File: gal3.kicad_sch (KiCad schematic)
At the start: 4 parts, among them IC13 SN74ALS374N, IC9 D65200GD076

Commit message: wire IC13
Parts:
- added C60: C_Small, Capacitor_SMD:C_1206_3216Metric, symbol Device:C_Small
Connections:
- net +5V: now also C60.1
- net GND: now also C60.2
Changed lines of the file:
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@@
   (junction (at 144.78 166.37) (diameter 0) (color 0 0 0 0)
+  )
+  (junction (at 95.25 137.16) (diameter 0) (color 0 0 0 0)
   )
   (junction (at 149.86 156.21) (diameter 0) (color 0 0 0 0)
@@
     (stroke (width 0) (type default))
   )
+  (wire (pts (xy 86.36 137.16) (xy 95.25 137.16))
+    (stroke (width 0) (type default))
+  )
   (wire (pts (xy 107.95 171.45) (xy 118.11 171.45))
     (stroke (width 0) (type default))
@@
     (stroke (width 0) (type default))
   )
+  (wire (pts (xy 86.36 140.97) (xy 86.36 142.24))
+    (stroke (width 0) (type default))
+  )
   (wire (pts (xy 139.7 151.13) (xy 167.64 151.13))
     (stroke (width 0) (type default))
@@
     (stroke (width 0) (type default))
   )
+  (wire (pts (xy 95.25 137.16) (xy 95.25 143.51))
+    (stroke (width 0) (type default))
+  )
   (wire (pts (xy 144.78 166.37) (xy 167.64 166.37))
     (stroke (width 0) (type default))
@@
   )
   (wire (pts (xy 152.4 142.24) (xy 152.4 158.75))
+    (stroke (width 0) (type default))
+  )
+  (wire (pts (xy 95.25 135.89) (xy 95.25 137.16))
     (stroke (width 0) (type default))
   )
@@
     )
   )
+  (symbol (lib_id "power:GND") (at 86.36 140.97 0) (unit 1)
+    (in_bom yes) (on_board yes) (dnp no) (fields_autoplaced)
+    (property "Reference" "#PWR034" (at 86.36 147.32 0)
+      (effects (font (size 1.27 1.27)) hide)
+    )
+    (property "Value" "GND" (at 86.36 146.05 0)
+      (effects (font (size 1.27 1.27)))
+    )
+    (property "Footprint" "" (at 86.36 140.97 0)
+      (effects (font (size 1.27 1.27)) hide)
+    )
+    (property "Datasheet" "" (at 86.36 140.97 0)
+      (effects (font (size 1.27 1.27)) hide)
+    )
+    (pin "1")
+    (instances
+      (project "88va2-circuit"
+        (path "/8cd193ae-a369-4130-9ba4-f2075fa60e2b/69b5e096-b79d-4084-a9d7-aa17e9aa2515"
+          (reference "#PWR034") (unit 1)
+        )
+      )
+    )
+  )
   (symbol (lib_id "power:+5V") (at 52.07 72.39 0) (unit 1)
     (in_bom yes) (on_board yes) (dnp no) (fields_autoplaced)
@@
     )
   )
+  (symbol (lib_id "Device:C_Small") (at 86.36 139.7 0) (unit 1)
+    (in_bom yes) (on_board yes) (dnp no) (fields_autoplaced)
+    (property "Reference" "C60" (at 88.9 139.7063 0)
+      (effects (font (size 1.27 1.27)) (justify left))
+    )
+    (property "Value" "C_Small" (at 88.9 140.9763 0)
+      (effects (font (size 1.27 1.27)) (justify left) hide)
+    )
+    (property "Footprint" "Capacitor_SMD:C_1206_3216Metric" (at 86.36 139.7 0)
+      (effects (font (size 1.27 1.27)) hide)
+    )
+    (property "Datasheet" "~" (at 86.36 139.7 0)
+      (effects (font (size 1.27 1.27)) hide)
+    )
+    (pin "2")
+    (pin "1")
+    (instances
+      (project "88va2-circuit"
+        (path "/8cd193ae-a369-4130-9ba4-f2075fa60e2b/69b5e096-b79d-4084-a9d7-aa17e9aa2515"
+          (reference "C60") (unit 1)
+        )
+      )
+    )
+  )
   (symbol (lib_id "power:+5V") (at 137.16 132.08 0) (unit 1)
     (in_bom yes) (on_board yes) (dnp no) (fields_autoplaced)
@@
     )
   )
-  (symbol (lib_id "power:+5V") (at 95.25 143.51 0) (unit 1)
-    (in_bom yes) (on_board yes) (dnp no) (fields_autoplaced)
-    (property "Reference" "#PWR032" (at 95.25 147.32 0)
-      (effects (font (size 1.27 1.27)) hide)
-    )
-    (property "Value" "+5V" (at 95.25 138.43 0)
+  (symbol (lib_id "power:+5V") (at 95.25 135.89 0) (unit 1)
+    (in_bom yes) (on_board yes) (dnp no) (fields_autoplaced)
+    (property "Reference" "#PWR032" (at 95.25 139.7 0)
+      (effects (font (size 1.27 1.27)) hide)
+    )
+    (property "Value" "+5V" (at 95.25 130.81 0)
       (effects (font (size 1.27 1.27)))
     )
-    (property "Footprint" "" (at 95.25 143.51 0)
-      (effects (font (size 1.27 1.27)) hide)
-    )
-    (property "Datasheet" "" (at 95.25 143.51 0)
-      (effects (font (size 1.27 1.27)) hide)
-    )
+    (property "Footprint" "" (at 95.25 135.89 0)
+      (effects (font (size 1.27 1.27)) hide)
+    )
+    (property "Datasheet" "" (at 95.25 135.89 0)
+      (effects (font (size 1.27 1.27)) hide)
+    )

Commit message: wire IC13
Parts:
- R18: footprint (none) -> Resistor_SMD:R_1206_3216Metric
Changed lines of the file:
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@@
       (effects (font (size 1.27 1.27)) (justify left) hide)
     )
-    (property "Footprint" "" (at 72.39 143.51 0)
+    (property "Footprint" "Resistor_SMD:R_1206_3216Metric" (at 72.39 143.51 0)
       (effects (font (size 1.27 1.27)) hide)
     )

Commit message: fix pitch of IC9 pads
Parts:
- IC9: footprint 88va_Library:QFP-160_28x28_Pitch0.635mm -> 88va_Library:QFP-160_27.8x27.8_Pitch0.65mm
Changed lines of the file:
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@@
       (effects (font (size 1.27 1.27)) (justify left))
     )
-    (property "Footprint" "88va_Library:QFP-160_28x28_Pitch0.635mm" (at 52.07 78.74 0)
+    (property "Footprint" "88va_Library:QFP-160_27.8x27.8_Pitch0.65mm" (at 52.07 78.74 0)
       (effects (font (size 1.27 1.27)) hide)
     )

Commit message: wire power lines
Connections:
- net +5V: now also IC9.1 (VDD); no longer IC9.81 (VDD)
- net GND: now also IC9.41 (GND), IC9.42 (GND); no longer IC9.79 (GND), IC9.80 (GND)
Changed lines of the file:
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@@
     (pin "44")
     (pin "50")
-    (pin "80")
+    (pin "1")
     (pin "48")
     (pin "51")
-    (pin "79")
-    (pin "81")
+    (pin "41")
+    (pin "42")
     (pin "69")
     (pin "140")

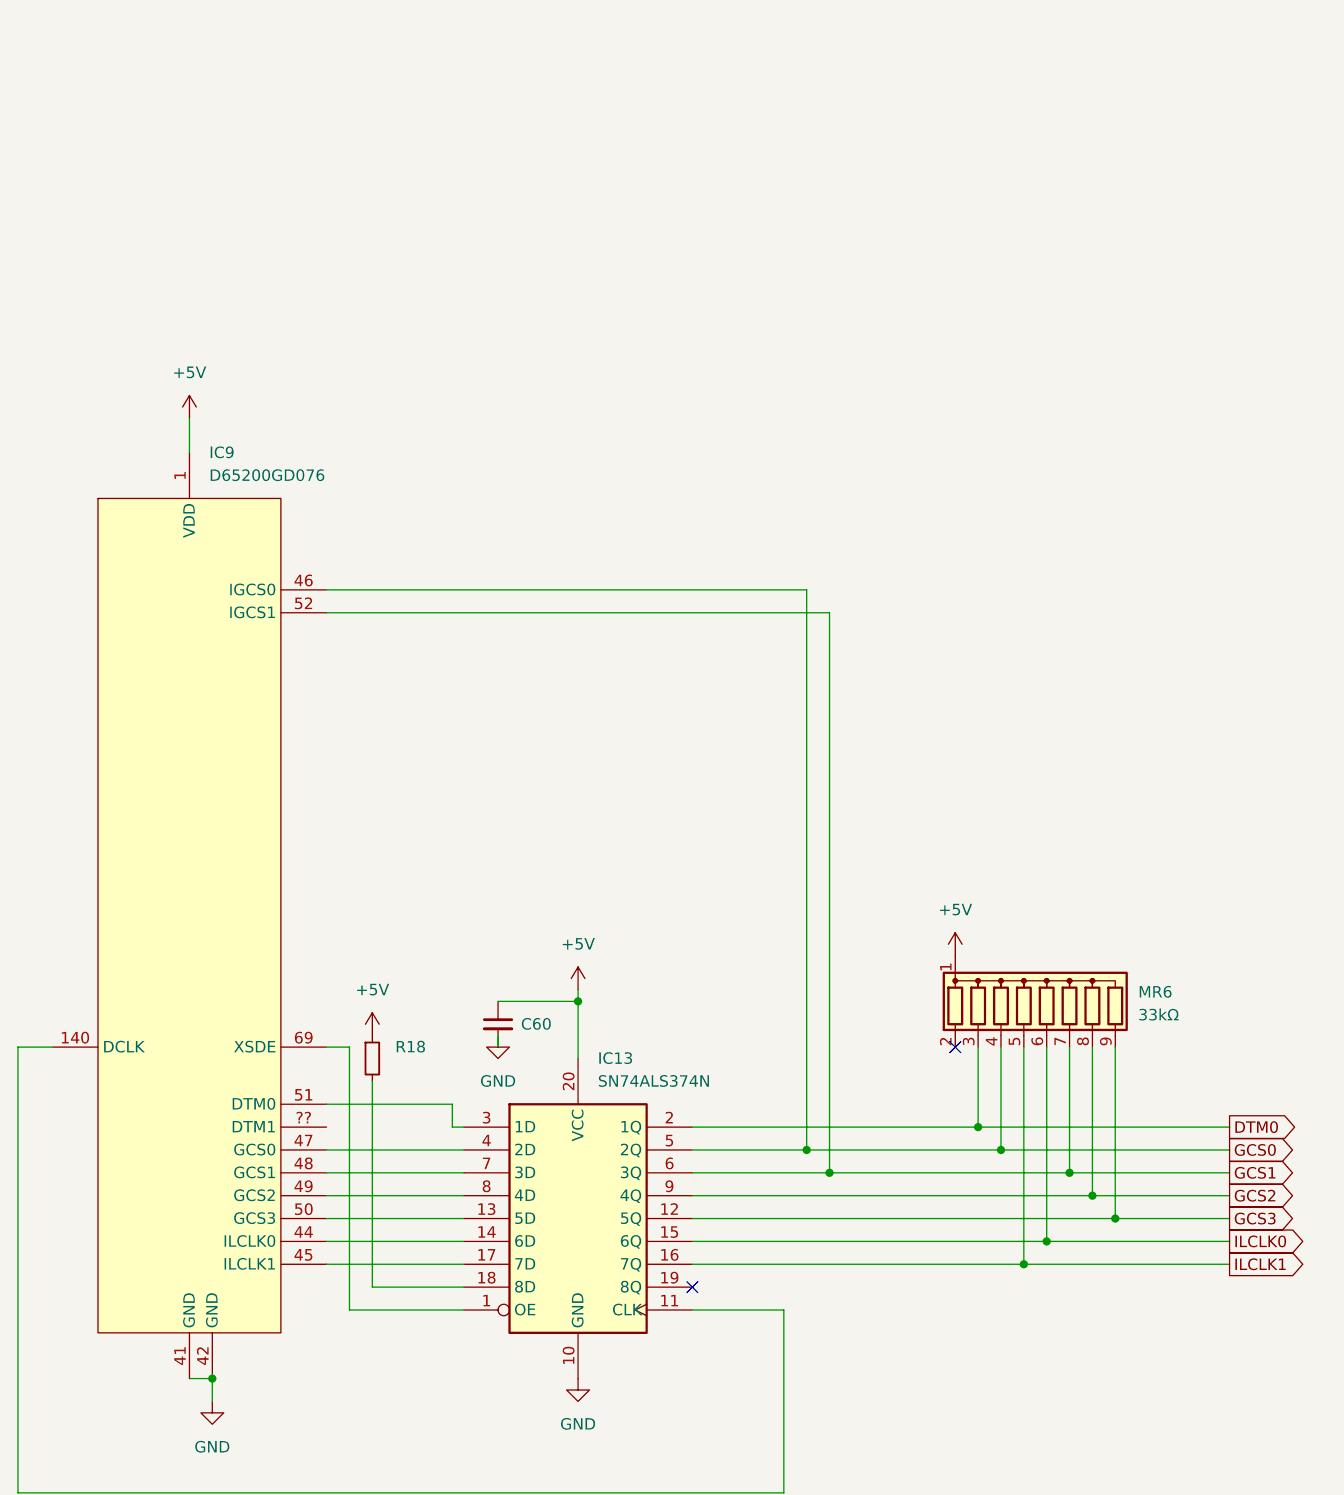
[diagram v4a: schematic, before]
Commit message: add IC8 to schematic
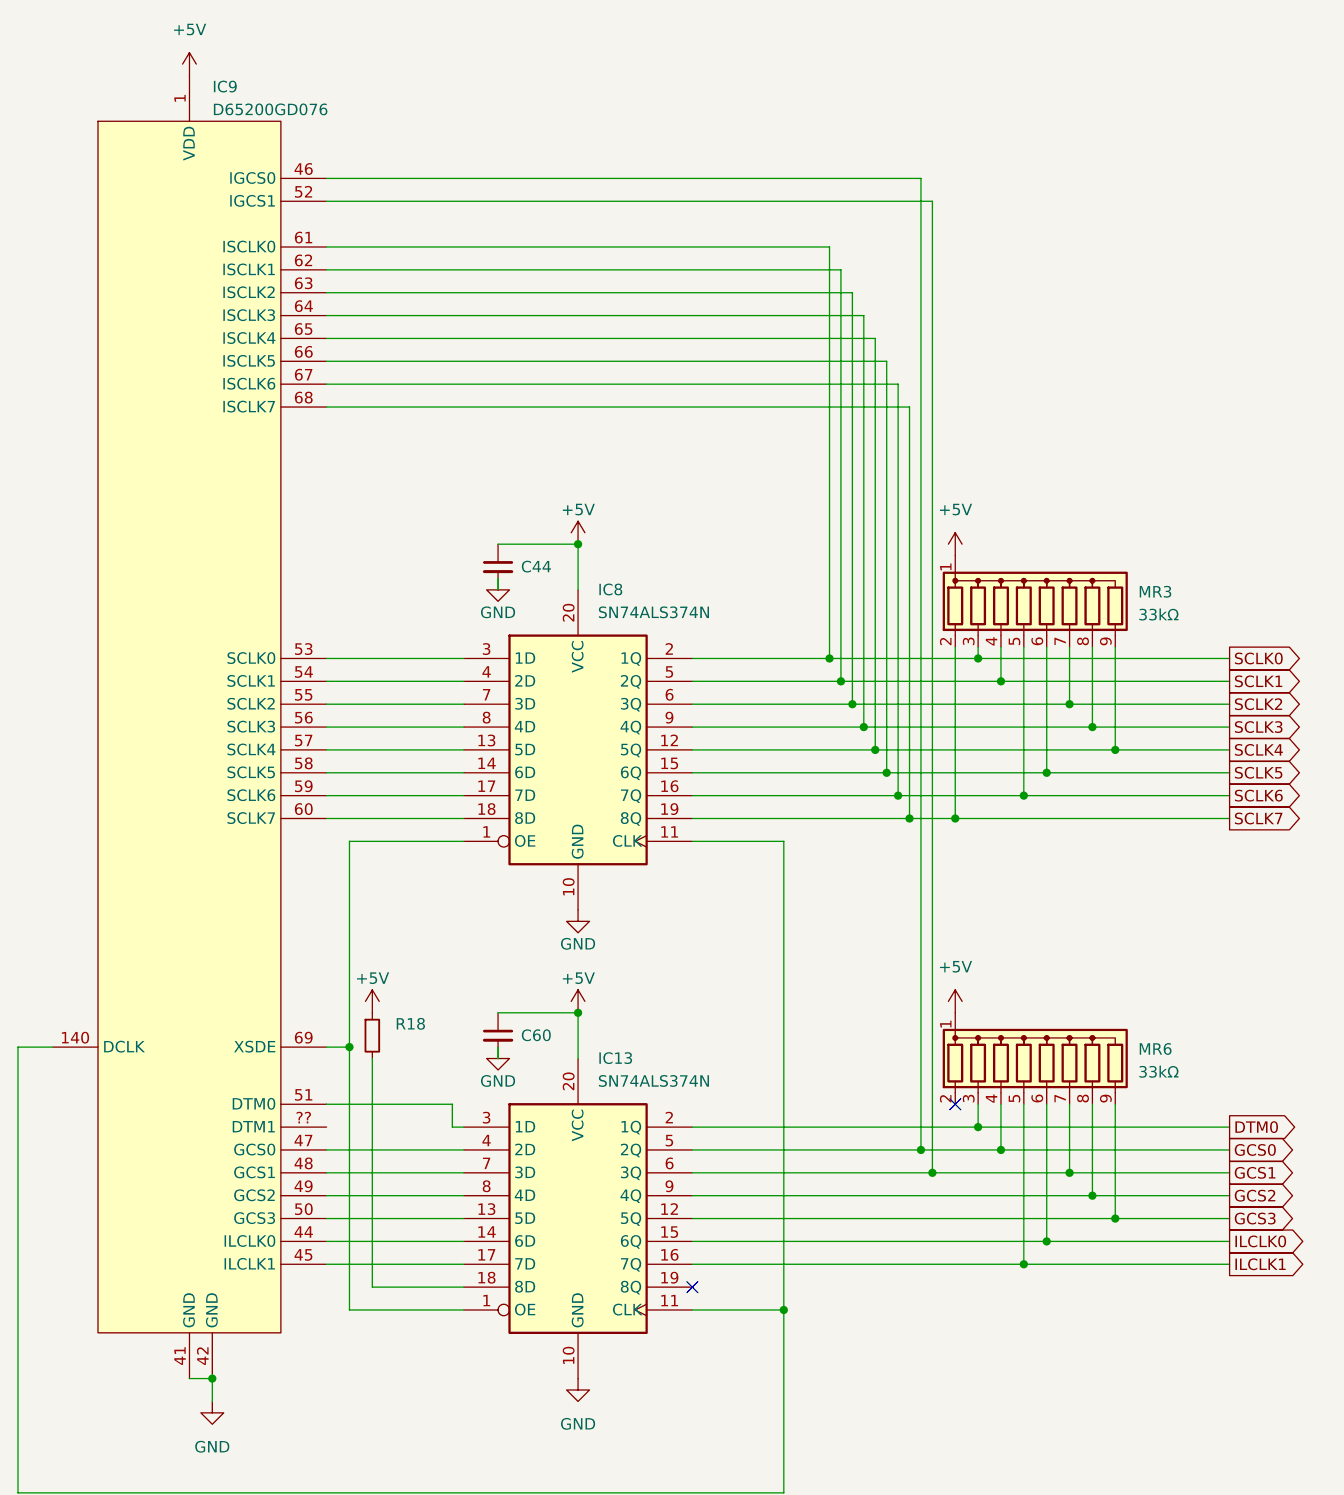
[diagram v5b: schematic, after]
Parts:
- added C44: C_Small, Capacitor_SMD:C_1206_3216Metric, symbol Device:C_Small
- added IC8: SN74ALS374N, Package_DIP:DIP-20_W7.62mm, symbol 88va_Library:74LS374
- added MR3: 33kΩ, Resistor_THT:R_Array_SIP9, symbol Device:R_Network08
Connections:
- net +5V: now also C44.1, IC8.20 (VCC), MR3.1 (common)
- net GND: now also C44.2, IC8.10 (GND)
- net at IC13.11 (CLK), IC9.140 (DCLK): now also IC8.11 (CLK)
- net at IC13.1 (OE), IC9.69 (XSDE): now also IC8.1 (OE)
- new net: IC8.3 (1D), IC9.53 (SCLK0)
- new net: IC8.4 (2D), IC9.54 (SCLK1)
- new net: IC8.7 (3D), IC9.55 (SCLK2)
- new net: IC8.8 (4D), IC9.56 (SCLK3)
- new net: IC8.13 (5D), IC9.57 (SCLK4)
- new net: IC8.14 (6D), IC9.58 (SCLK5)
- new net: IC8.17 (7D), IC9.59 (SCLK6)
- new net: IC8.18 (8D), IC9.60 (SCLK7)
- new net SCLK0: IC8.2 (1Q), IC9.61 (ISCLK0), MR3.3 (R2)
- new net SCLK1: IC8.5 (2Q), IC9.62 (ISCLK1), MR3.4 (R3)
- new net SCLK2: IC8.6 (3Q), IC9.63 (ISCLK2), MR3.7 (R6)
- new net SCLK3: IC8.9 (4Q), IC9.64 (ISCLK3), MR3.8 (R7)
- new net SCLK4: IC8.12 (5Q), IC9.65 (ISCLK4), MR3.9 (R8)
- new net SCLK5: IC8.15 (6Q), IC9.66 (ISCLK5), MR3.6 (R5)
- new net SCLK6: IC8.16 (7Q), IC9.67 (ISCLK6), MR3.5 (R4)
- new net SCLK7: IC8.19 (8Q), IC9.68 (ISCLK7), MR3.2 (R1)
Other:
- moved on the sheet: C60, MR6, R18

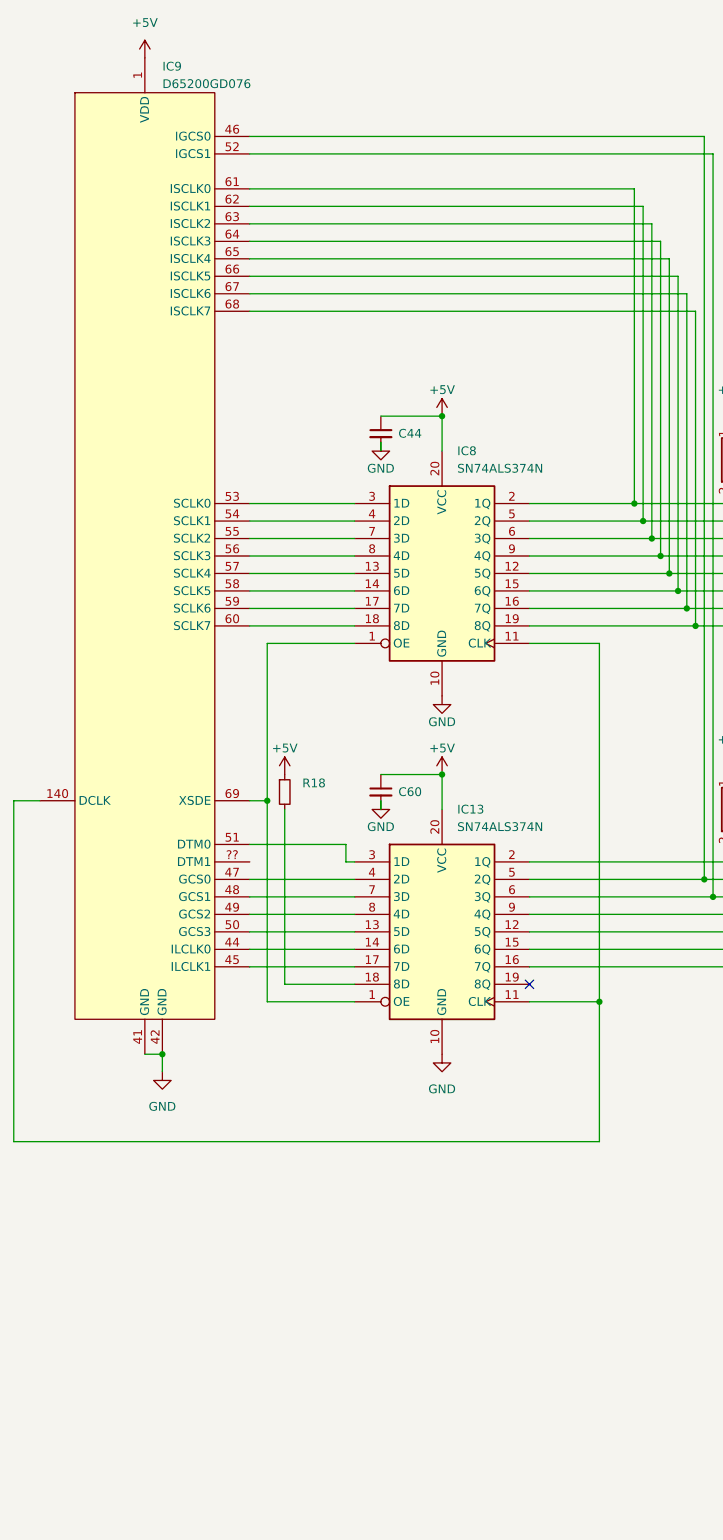
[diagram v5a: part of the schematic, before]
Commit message: wiring IC9
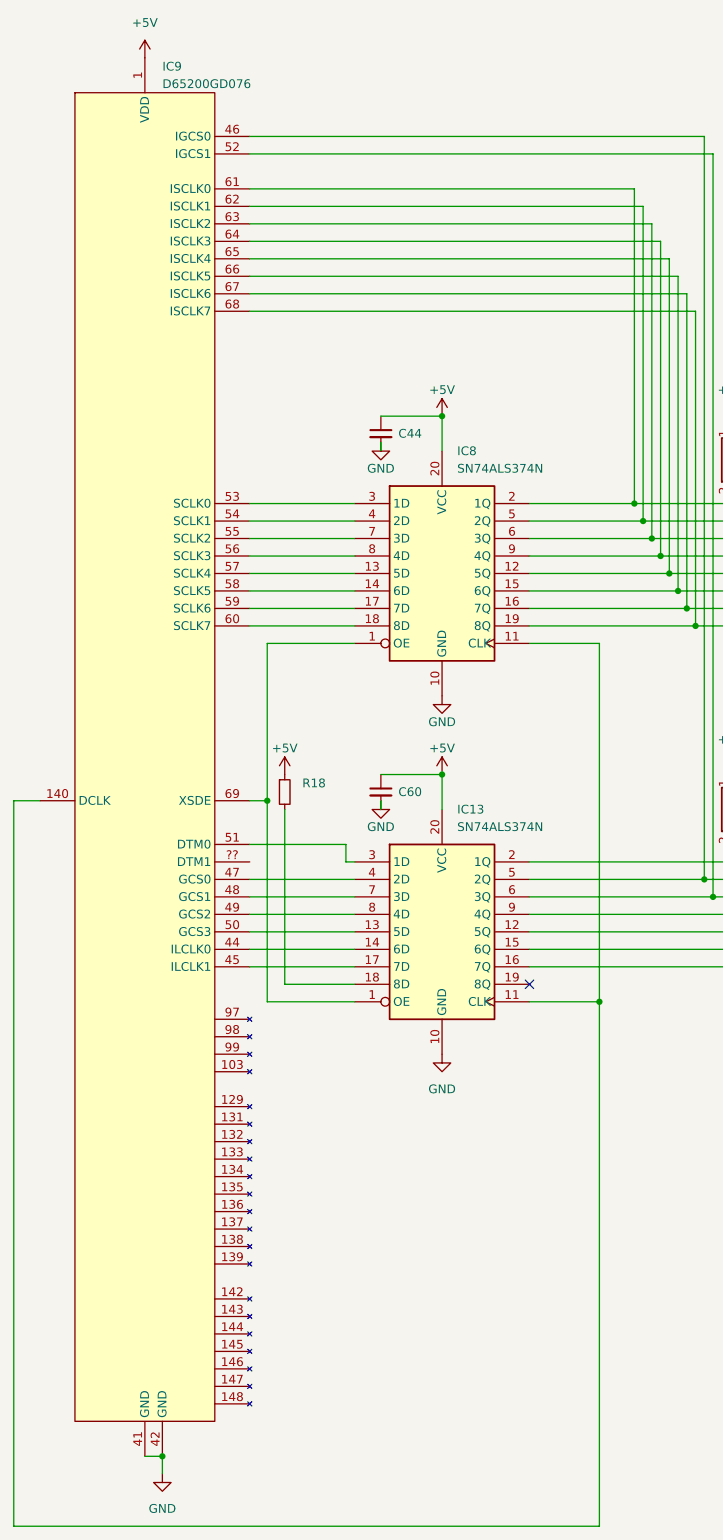
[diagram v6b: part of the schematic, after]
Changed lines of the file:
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@@
 (kicad_sch (version 20230121) (generator eeschema)
-  (paper "A4")
+  (paper "A3" portrait)
   (junction (at 123.19 99.06) (diameter 0) (color 0 0 0 0)
   )
@@
   (junction (at 139.7 99.06) (diameter 0) (color 0 0 0 0)
   )
-  (junction (at 54.61 179.07) (diameter 0) (color 0 0 0 0)
+  (junction (at 54.61 237.49) (diameter 0) (color 0 0 0 0)
   )
   (no_connect (at 107.95 168.91))
@@
     (stroke (width 0) (type default))
   )
-  (wire (pts (xy 52.07 179.07) (xy 54.61 179.07))
-    (stroke (width 0) (type default))
-  )
-  (wire (pts (xy 118.11 191.77) (xy 33.02 191.77))
+  (wire (pts (xy 52.07 237.49) (xy 54.61 237.49))
+    (stroke (width 0) (type default))
+  )
+  (wire (pts (xy 118.11 247.65) (xy 33.02 247.65))
     (stroke (width 0) (type default))
   )
@@
     (stroke (width 0) (type default))
   )
-  (wire (pts (xy 33.02 191.77) (xy 33.02 142.24))
+  (wire (pts (xy 33.02 247.65) (xy 33.02 142.24))
     (stroke (width 0) (type default))
   )
@@
     (stroke (width 0) (type default))
   )
-  (wire (pts (xy 54.61 179.07) (xy 54.61 181.61))
+  (wire (pts (xy 54.61 237.49) (xy 54.61 240.03))
     (stroke (width 0) (type default))
   )
@@
     (stroke (width 0) (type default))
   )
-  (wire (pts (xy 118.11 171.45) (xy 118.11 191.77))
+  (wire (pts (xy 118.11 171.45) (xy 118.11 247.65))
     (stroke (width 0) (type default))
   )
@@
     (pin "62")
     (pin "65")
+    (pin "103")
+    (pin "129")
+    (pin "132")
+    (pin "131")
+    (pin "133")
+    (pin "134")
+    (pin "135")
+    (pin "136")
+    (pin "137")
+    (pin "97")
+    (pin "142")
+    (pin "99")
+    (pin "147")
+    (pin "143")
+    (pin "139")
+    (pin "138")
+    (pin "145")
+    (pin "148")
+    (pin "98")
+    (pin "146")
+    (pin "144")
     (instances
       (project "88va2-circuit"
@@
     )
   )
-  (symbol (lib_id "power:GND") (at 54.61 181.61 0) (unit 1)
+  (symbol (lib_id "power:GND") (at 54.61 240.03 0) (unit 1)
     (in_bom yes) (on_board yes) (dnp no) (fields_autoplaced)
-    (property "Reference" "#PWR025" (at 54.61 187.96 0)
-      (effects (font (size 1.27 1.27)) hide)
-    )
-    (property "Value" "GND" (at 54.61 186.69 0)
+    (property "Reference" "#PWR025" (at 54.61 246.38 0)
+      (effects (font (size 1.27 1.27)) hide)
+    )
+    (property "Value" "GND" (at 54.61 245.11 0)
       (effects (font (size 1.27 1.27)))
     )
-    (property "Footprint" "" (at 54.61 181.61 0)
-      (effects (font (size 1.27 1.27)) hide)
-    )
-    (property "Datasheet" "" (at 54.61 181.61 0)
-      (effects (font (size 1.27 1.27)) hide)
-    )
+    (property "Footprint" "" (at 54.61 240.03 0)
+      (effects (font (size 1.27 1.27)) hide)
+    )
+    (property "Datasheet" "" (at 54.61 240.03 0)
+      (effects (font (size 1.27 1.27)) hide)
+    )
